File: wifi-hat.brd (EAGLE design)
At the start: 65 x 30 mm, 16 parts

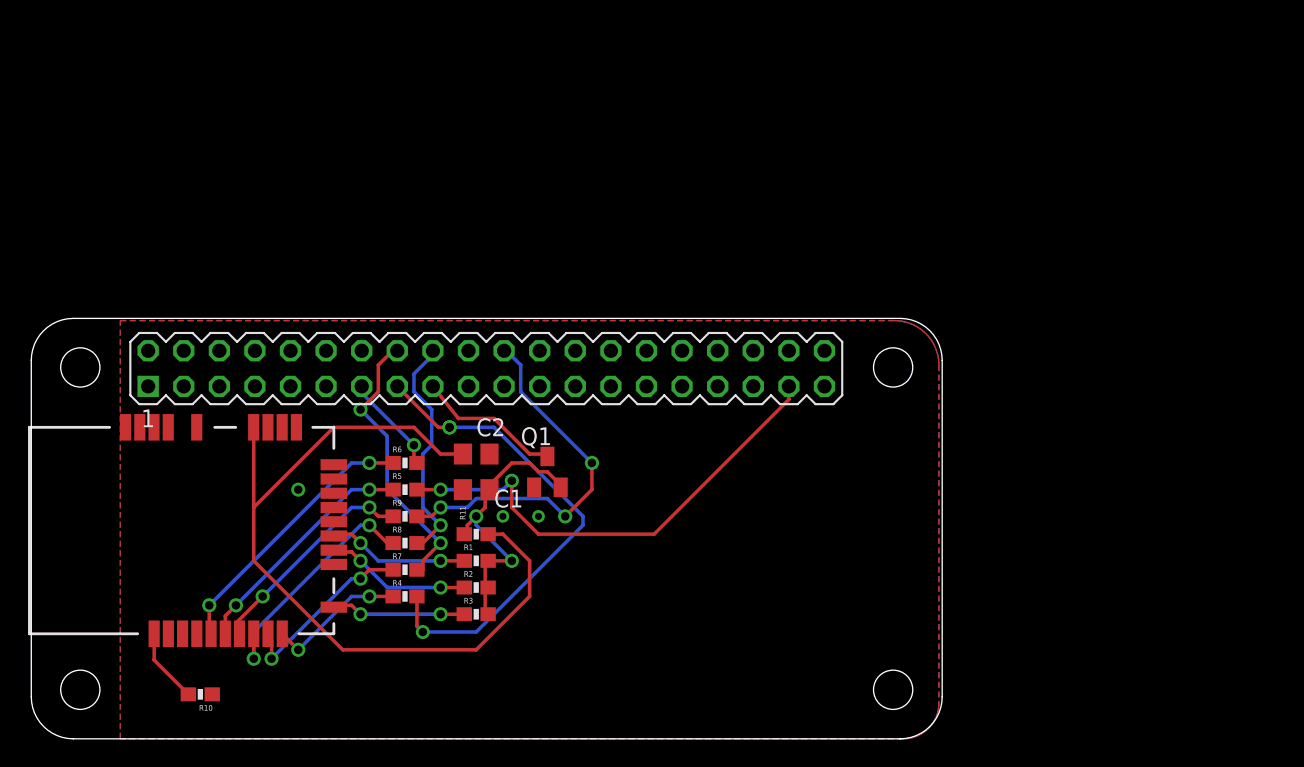
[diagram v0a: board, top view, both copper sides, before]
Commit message: cleanup and fixes
Cleaned up the board and schematic layouts. Connected RESET_N to GPIO to handle power cycling.
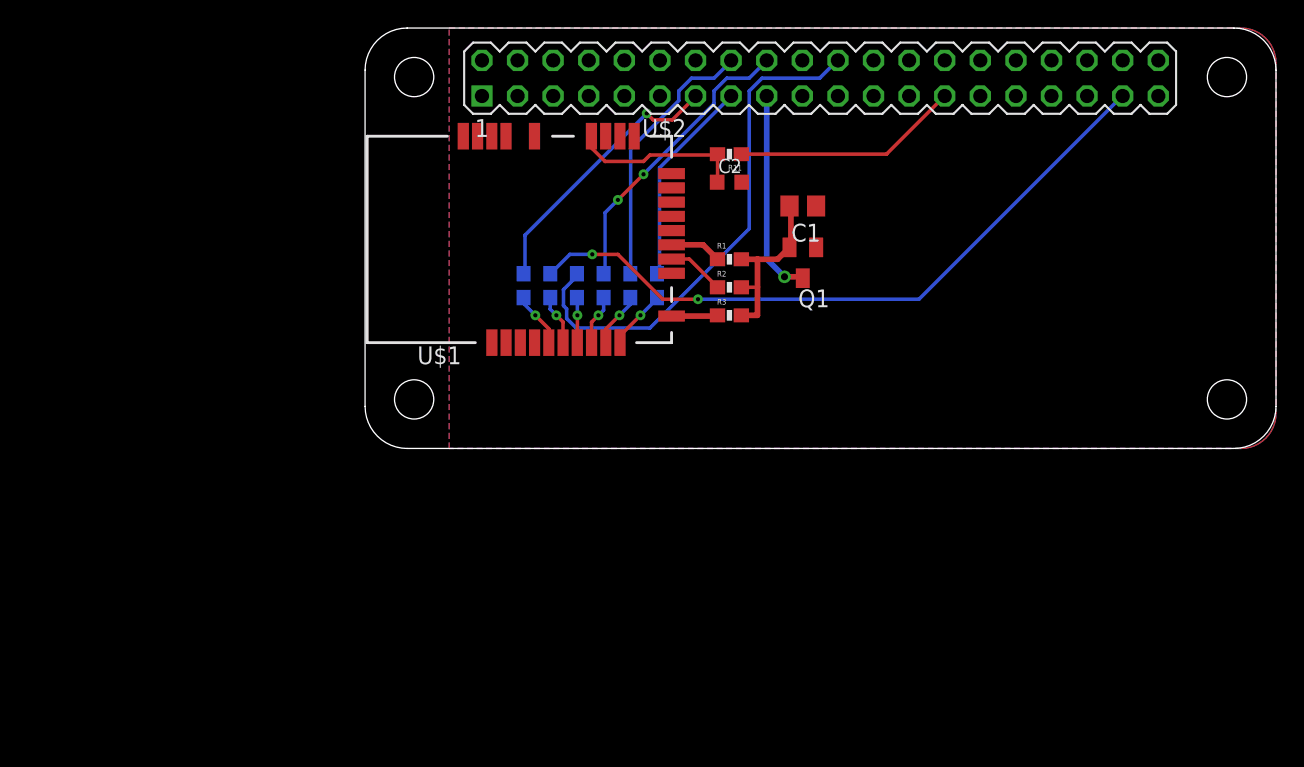
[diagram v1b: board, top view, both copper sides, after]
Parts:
- removed R10: 0 Ohm, SparkFun-Resistors:0603-RES
- C2: device sym:C0805 -> resistor:C0603K
- U$2: value PIZERO -> PIZERO_THROUGH_HOLE
- moved R11 32.6 mm to (93.0, 59.5), turned to 180 degrees
- moved U$1 31.8 mm to (88.9, 60.8)
- moved U$2 31.6 mm to (67.0, 38.5)
- moved C1 30.9 mm to (98.2, 55.8), turned to 180 degrees
- moved R4 28.6 mm to (87.8, 50.1), flipped to the bottom, turned to 90 degrees
- moved R1 28.1 mm to (93.0, 52.0)
- moved R2 28.0 mm to (93.0, 50.0)
- moved R3 28.0 mm to (93.0, 48.0)
- moved C2 26.5 mm to (93.0, 57.5)
- moved R7 25.9 mm to (85.9, 50.1), flipped to the bottom, turned to 90 degrees
- moved Q1 23.6 mm to (98.2, 51.8), turned to 180 degrees
- moved R8 23.2 mm to (84.0, 50.1), flipped to the bottom, turned to 90 degrees
- moved R9 20.5 mm to (82.1, 50.1), flipped to the bottom, turned to 90 degrees
- moved R5 17.9 mm to (80.2, 50.1), flipped to the bottom, turned to 90 degrees
- moved R6 15.2 mm to (78.3, 50.1), flipped to the bottom, turned to 90 degrees
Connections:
- net 3V3 renamed 3.3V
- net N$11 renamed SD_DAT2
- net N$12 renamed SD_CMD
- net N$13 renamed SD_DAT0
- net N$14 renamed SD_DAT1
- net N$9 renamed RESET_N
- net R6 renamed SD_DAT3
- removed net S$2: R4.2, U$2.15
- removed net SDIO_CFG: R10.2, U$1.10
- new net ID_SD: R11.1, U$2.27
- new net N$23: R4.1, U$1.19
- net GND: now also U$1.10; no longer R10.1
- net SD_CLK: now also R4.2, U$2.15; no longer R4.1, U$1.19
- net VCC: no longer R11.1
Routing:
- net RESET_N: track 57.8 -> 12.4 mm
- net S$2: track 35.0 -> 0.00 mm, vias 2 -> 0
- net ID_SD: track 0.00 -> 16.2 mm
- net N$8: track 19.4 -> 3.97 mm, vias 2 -> 1
- net SD_DAT2: track 34.4 -> 48.7 mm
- net N$5: track 17.3 -> 3.58 mm, vias 2 -> 1
- net N$7: track 17.0 -> 3.60 mm, vias 2 -> 1
- net N$6: track 15.8 -> 3.35 mm, vias 2 -> 1
- net SD_DAT3: track 7.27 -> 19.5 mm
- net SD_DAT1: track 26.9 -> 37.0 mm, vias 3 -> 0
- net N$4: track 13.1 -> 3.95 mm, vias 2 -> 1
- net VCC: track 21.6 -> 13.2 mm, vias 2 -> 0
- net N$2: track 10.2 -> 3.71 mm, vias 2 -> 0
- net N$3: track 9.70 -> 3.30 mm, vias 2 -> 0
- net N$1: track 10.5 -> 4.11 mm, vias 2 -> 0
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
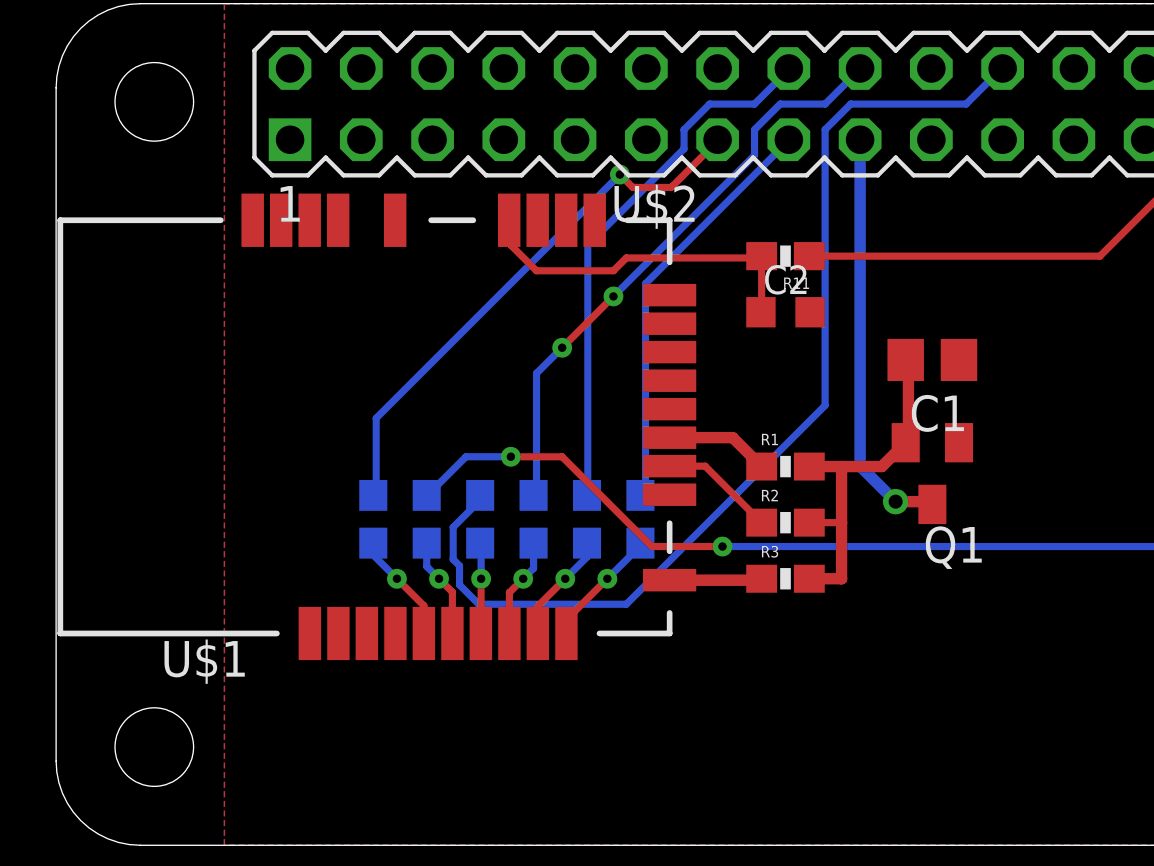
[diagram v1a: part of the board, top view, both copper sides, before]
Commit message: Replace Caps with 603 variants
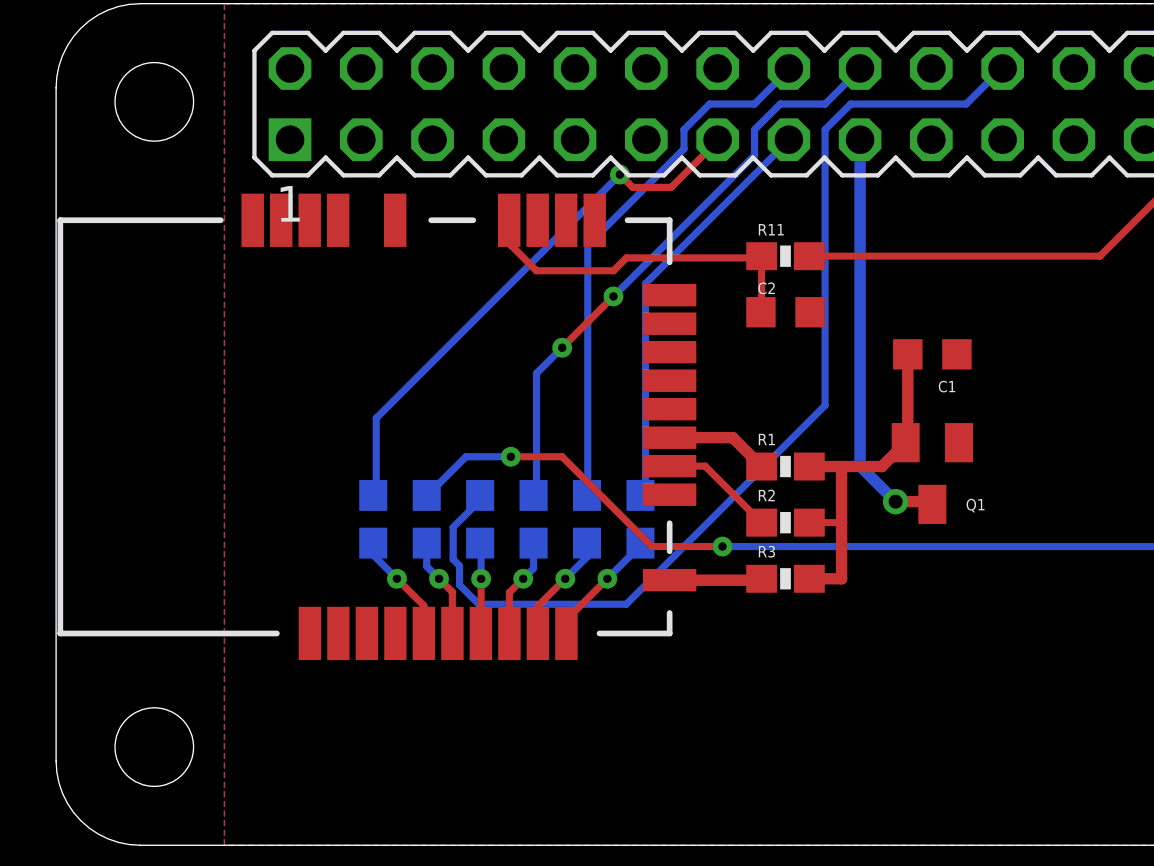
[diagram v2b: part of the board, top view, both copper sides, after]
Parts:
- C1: device sym:C0805 -> resistor:C0603K
- Q1: value (none) -> NDS332P
- moved C1 0.20 mm to (98.2, 56.0), turned to 0 degrees
- renumbered U$1 to WI_SOC
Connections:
- net GND: now also C1.2; no longer C1.1
- net VCC: now also C1.1; no longer C1.2
